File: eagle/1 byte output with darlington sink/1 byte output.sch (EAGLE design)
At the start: 13 parts, among them IC1 74LS595N, IC2 74LS595N, X1 MKDSN1,5/8-5,08, X2 MKDSN1,5/8-5,08, X5 MKDSN1,5/2-5,08

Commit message: periodic check-in
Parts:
- removed C1: (no value), resistor:C-EU050-035X075
- removed IC2: 74LS595N, 74xx-us:74LS595N
- removed ULN2: uln2803, SparkFun-IC-Special-Function:ULN2803DIP
- removed X2: MKDSN1,5/8-5,08, con-phoenix-508:MKDSN1,5/8-5,08
- ULN2803: value ULN2803 -> (none)
- renumbered ULN1 to ULN2803
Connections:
- removed net DP: IC1A.QH*, IC2A.SER
- removed net N$10: ULN2.17, X2-2.KL
- removed net N$11: ULN2.16, X2-3.KL
- removed net N$12: ULN2.15, X2-4.KL
- removed net N$13: ULN2.14, X2-5.KL
- removed net N$14: ULN2.13, X2-6.KL
- removed net N$15: ULN2.12, X2-7.KL
- removed net N$16: ULN2.11, X2-8.KL
- removed net N$9: ULN2.18, X2-1.KL
- removed net OUT10: IC2A.QC, ULN2.3
- removed net OUT11: IC2A.QD, ULN2.4
- removed net OUT12: IC2A.QE, ULN2.5
- removed net OUT13: IC2A.QF, ULN2.6
- removed net OUT14: IC2A.QG, ULN2.7
- removed net OUT15: IC2A.QH, ULN2.8
- removed net OUT8: IC2A.QA, ULN2.1
- removed net OUT9: IC2A.QB, ULN2.2
- net CLK: no longer IC2A.SCK
- net COM: no longer ULN2.10
- net DO: now also IC1A.QH*; no longer IC2A.QH*
- net GND: no longer C1.2, IC2A.G, IC2P.GND, ULN2.9
- net LATCH: no longer IC2A.RCK
- net VCC: no longer C1.1, IC2A.SCL, IC2P.VCC

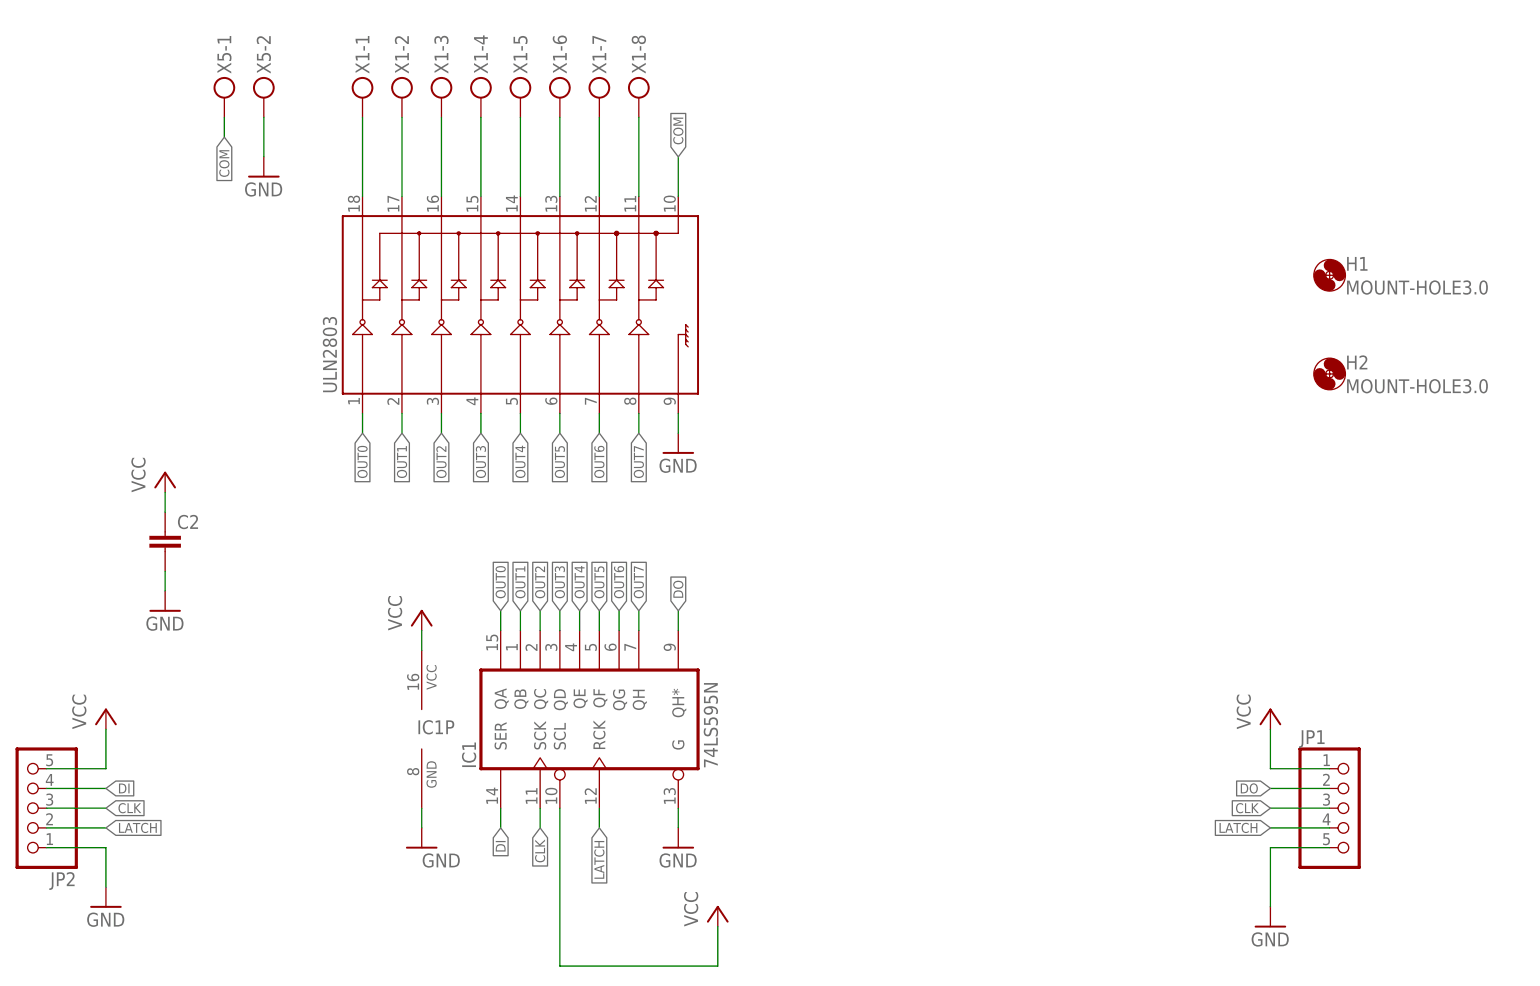
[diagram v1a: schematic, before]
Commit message: added pdf file of schematics and boards, removed button debounce and servo driver
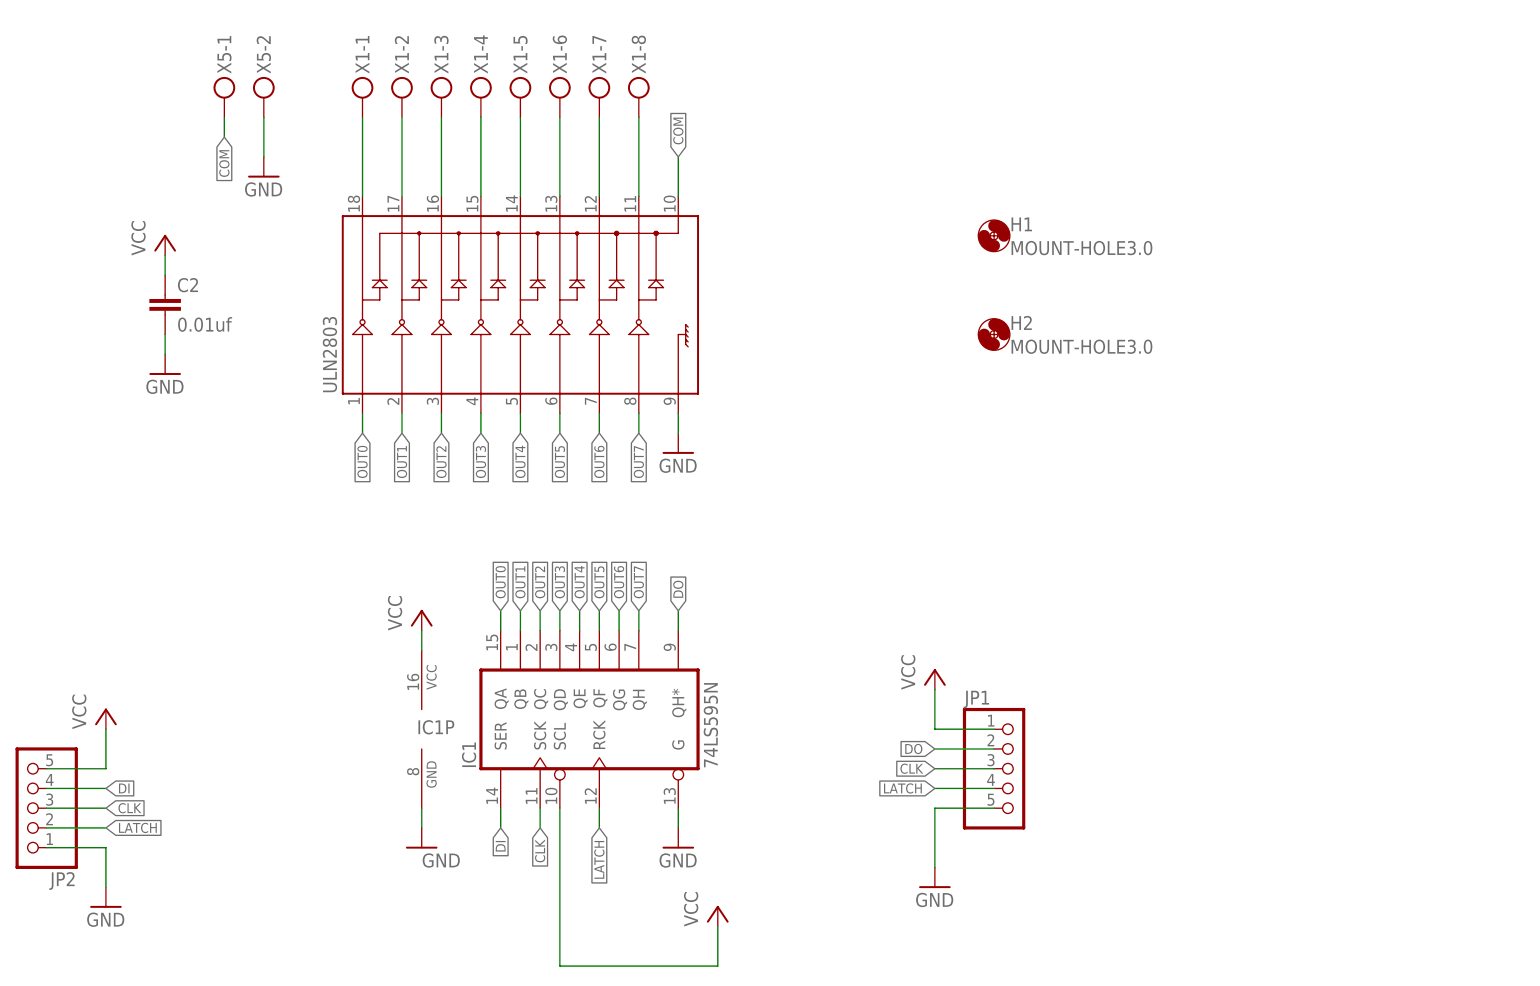
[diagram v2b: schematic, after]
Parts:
- C2: value (none) -> 0.01uf
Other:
- moved on the sheet: C2, H1, H2, JP1
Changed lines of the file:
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@@
 <?xml version="1.0" encoding="utf-8"?>
 <!DOCTYPE eagle SYSTEM "eagle.dtd">
-<eagle version="9.4.2">
+<eagle version="9.5.0">
 <drawing>
 <settings>
@@
 <part name="GND8" library="supply1" library_urn="urn:adsk.eagle:library:371" deviceset="GND" device=""/>
 <part name="P+7" library="supply1" library_urn="urn:adsk.eagle:library:371" deviceset="VCC" device=""/>
-<part name="C2" library="resistor" library_urn="urn:adsk.eagle:library:348" deviceset="C-EU" device="050-035X075" package3d_urn="urn:adsk.eagle:package:23677/1"/>
+<part name="C2" library="resistor" library_urn="urn:adsk.eagle:library:348" deviceset="C-EU" device="050-035X075" package3d_urn="urn:adsk.eagle:package:23677/1" value="0.01uf"/>
 <part name="P+1" library="supply1" library_urn="urn:adsk.eagle:library:371" deviceset="VCC" device=""/>
 <part name="GND1" library="supply1" library_urn="urn:adsk.eagle:library:371" deviceset="GND" device=""/>
@@
 <part name="GND3" library="supply1" library_urn="urn:adsk.eagle:library:371" deviceset="GND" device=""/>
 <part name="JP1" library="pinhead" library_urn="urn:adsk.eagle:library:325" deviceset="PINHD-1X5" device="/90" package3d_urn="urn:adsk.eagle:package:22467/2"/>
+<part name="FRAME1" library="frames" library_urn="urn:adsk.eagle:library:229" deviceset="LETTER_L" device=""/>
 </parts>
 <sheets>
@@
 <attribute name="VALUE" x="53.34" y="20.32" size="1.778" layer="96" rot="R90"/>
 </instance>
-<instance part="C2" gate="G$1" x="-15.24" y="71.12" smashed="yes">
-<attribute name="NAME" x="-13.716" y="71.501" size="1.778" layer="95"/>
-<attribute name="VALUE" x="-13.716" y="66.421" size="1.778" layer="96"/>
-</instance>
-<instance part="P+1" gate="VCC" x="-15.24" y="78.74" smashed="yes">
-<attribute name="VALUE" x="-17.78" y="76.2" size="1.778" layer="96" rot="R90"/>
-</instance>
-<instance part="GND1" gate="1" x="-15.24" y="60.96" smashed="yes">
-<attribute name="VALUE" x="-17.78" y="58.42" size="1.778" layer="96"/>
+<instance part="C2" gate="G$1" x="-15.24" y="101.6" smashed="yes">
+<attribute name="NAME" x="-13.716" y="101.981" size="1.778" layer="95"/>
+<attribute name="VALUE" x="-13.716" y="96.901" size="1.778" layer="96"/>
+</instance>
+<instance part="P+1" gate="VCC" x="-15.24" y="109.22" smashed="yes">
+<attribute name="VALUE" x="-17.78" y="106.68" size="1.778" layer="96" rot="R90"/>
+</instance>
+<instance part="GND1" gate="1" x="-15.24" y="91.44" smashed="yes">
+<attribute name="VALUE" x="-17.78" y="88.9" size="1.778" layer="96"/>
 </instance>
 <instance part="ULN2803" gate="G$1" x="27.94" y="99.06" smashed="yes" rot="R90">
@@
 <attribute name="VALUE" x="48.26" y="78.74" size="1.778" layer="96"/>
 </instance>
-<instance part="H1" gate="G$1" x="134.62" y="104.14" smashed="yes">
-<attribute name="NAME" x="136.652" y="104.7242" size="1.778" layer="95"/>
-<attribute name="VALUE" x="136.652" y="101.6762" size="1.778" layer="96"/>
-</instance>
-<instance part="H2" gate="G$1" x="134.62" y="91.44" smashed="yes">
-<attribute name="NAME" x="136.652" y="92.0242" size="1.778" layer="95"/>
-<attribute name="VALUE" x="136.652" y="88.9762" size="1.778" layer="96"/>
-</instance>
-<instance part="P+8" gate="VCC" x="127" y="48.26" smashed="yes">
-<attribute name="VALUE" x="124.46" y="45.72" size="1.778" layer="96" rot="R90"/>
-</instance>
-<instance part="GND12" gate="1" x="127" y="20.32" smashed="yes">
-<attribute name="VALUE" x="124.46" y="17.78" size="1.778" layer="96"/>
+<instance part="H1" gate="G$1" x="91.44" y="109.22" smashed="yes">
+<attribute name="NAME" x="93.472" y="109.8042" size="1.778" layer="95"/>
+<attribute name="VALUE" x="93.472" y="106.7562" size="1.778" layer="96"/>
+</instance>
+<instance part="H2" gate="G$1" x="91.44" y="96.52" smashed="yes">
+<attribute name="NAME" x="93.472" y="97.1042" size="1.778" layer="95"/>
+<attribute name="VALUE" x="93.472" y="94.0562" size="1.778" layer="96"/>
+</instance>
+<instance part="P+8" gate="VCC" x="83.82" y="53.34" smashed="yes">
+<attribute name="VALUE" x="81.28" y="50.8" size="1.778" layer="96" rot="R90"/>
+</instance>
+<instance part="GND12" gate="1" x="83.82" y="25.4" smashed="yes">
+<attribute name="VALUE" x="81.28" y="22.86" size="1.778" layer="96"/>
 </instance>
 <instance part="JP2" gate="A" x="-33.02" y="35.56" smashed="yes" rot="R180">
@@
 <attribute name="VALUE" x="-25.4" y="20.32" size="1.778" layer="96"/>
 </instance>
-<instance part="JP1" gate="A" x="137.16" y="35.56" smashed="yes">
-<attribute name="NAME" x="130.81" y="43.815" size="1.778" layer="95"/>
-<attribute name="VALUE" x="130.81" y="25.4" size="1.778" layer="96"/>
+<instance part="JP1" gate="A" x="93.98" y="40.64" smashed="yes">
+<attribute name="NAME" x="87.63" y="48.895" size="1.778" layer="95"/>
+<attribute name="VALUE" x="87.63" y="30.48" size="1.778" layer="96"/>
+</instance>
+<instance part="FRAME1" gate="G$1" x="-73.66" y="-33.02" smashed="yes"/>
+<instance part="FRAME1" gate="G$2" x="73.66" y="-33.02" smashed="yes">
+<attribute name="LAST_DATE_TIME" x="86.36" y="-31.75" size="2.54" layer="94"/>
+<attribute name="SHEET" x="160.02" y="-31.75" size="2.54" layer="94"/>
+<attribute name="DRAWING_NAME" x="91.44" y="-13.97" size="2.54" layer="94"/>
 </instance>
 </instances>
@@
 </segment>
 <segment>
-<wire x1="134.62" y1="35.56" x2="127" y2="35.56" width="0.1524" layer="91"/>
-<label x="127" y="35.56" size="1.27" layer="95" rot="MR0" xref="yes"/>
+<wire x1="91.44" y1="40.64" x2="83.82" y2="40.64" width="0.1524" layer="91"/>
+<label x="83.82" y="40.64" size="1.27" layer="95" rot="MR0" xref="yes"/>
 <pinref part="JP1" gate="A" pin="3"/>
 </segment>
@@
 </segment>
 <segment>
-<wire x1="134.62" y1="33.02" x2="127" y2="33.02" width="0.1524" layer="91"/>
-<label x="127" y="33.02" size="1.27" layer="95" rot="MR0" xref="yes"/>
+<wire x1="91.44" y1="38.1" x2="83.82" y2="38.1" width="0.1524" layer="91"/>
+<label x="83.82" y="38.1" size="1.27" layer="95" rot="MR0" xref="yes"/>
 <pinref part="JP1" gate="A" pin="4"/>
 </segment>
@@
 <net name="DO" class="0">
 <segment>
-<wire x1="134.62" y1="38.1" x2="127" y2="38.1" width="0.1524" layer="91"/>
-<label x="127" y="38.1" size="1.27" layer="95" rot="MR0" xref="yes"/>
+<wire x1="91.44" y1="43.18" x2="83.82" y2="43.18" width="0.1524" layer="91"/>
+<label x="83.82" y="43.18" size="1.27" layer="95" rot="MR0" xref="yes"/>
 <pinref part="JP1" gate="A" pin="2"/>
 </segment>
@@
 <segment>
 <pinref part="C2" gate="G$1" pin="1"/>
-<wire x1="-15.24" y1="73.66" x2="-15.24" y2="76.2" width="0.1524" layer="91"/>
+<wire x1="-15.24" y1="104.14" x2="-15.24" y2="106.68" width="0.1524" layer="91"/>
 <pinref part="P+1" gate="VCC" pin="VCC"/>
 </segment>
 <segment>
-<wire x1="134.62" y1="40.64" x2="127" y2="40.64" width="0.1524" layer="91"/>
-<wire x1="127" y1="40.64" x2="127" y2="45.72" width="0.1524" layer="91"/>
+<wire x1="91.44" y1="45.72" x2="83.82" y2="45.72" width="0.1524" layer="91"/>
+<wire x1="83.82" y1="45.72" x2="83.82" y2="50.8" width="0.1524" layer="91"/>
 <pinref part="P+8" gate="VCC" pin="VCC"/>
 <pinref part="JP1" gate="A" pin="1"/>
@@
 <segment>
 <pinref part="C2" gate="G$1" pin="2"/>
-<wire x1="-15.24" y1="66.04" x2="-15.24" y2="63.5" width="0.1524" layer="91"/>
+<wire x1="-15.24" y1="96.52" x2="-15.24" y2="93.98" width="0.1524" layer="91"/>
 <pinref part="GND1" gate="1" pin="GND"/>
 </segment>
@@
 </segment>
 <segment>
-<wire x1="134.62" y1="30.48" x2="127" y2="30.48" width="0.1524" layer="91"/>
-<wire x1="127" y1="30.48" x2="127" y2="22.86" width="0.1524" layer="91"/>
+<wire x1="91.44" y1="35.56" x2="83.82" y2="35.56" width="0.1524" layer="91"/>
+<wire x1="83.82" y1="35.56" x2="83.82" y2="27.94" width="0.1524" layer="91"/>
 <pinref part="GND12" gate="1" pin="GND"/>
 <pinref part="JP1" gate="A" pin="5"/>
